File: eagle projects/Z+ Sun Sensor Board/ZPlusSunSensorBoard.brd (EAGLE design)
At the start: 91 x 91 mm, 53 parts, among them Q1 BSS138PS,115, Q2 BSS138PS,115, Q7 BSS138PS,115, Q8 BSS138PS,115, U1 ADS7841E_2K5, U2 REF194GSZ-REEL7, U3 TLV9054IDR, U4 LM20BIM7X_NOPB

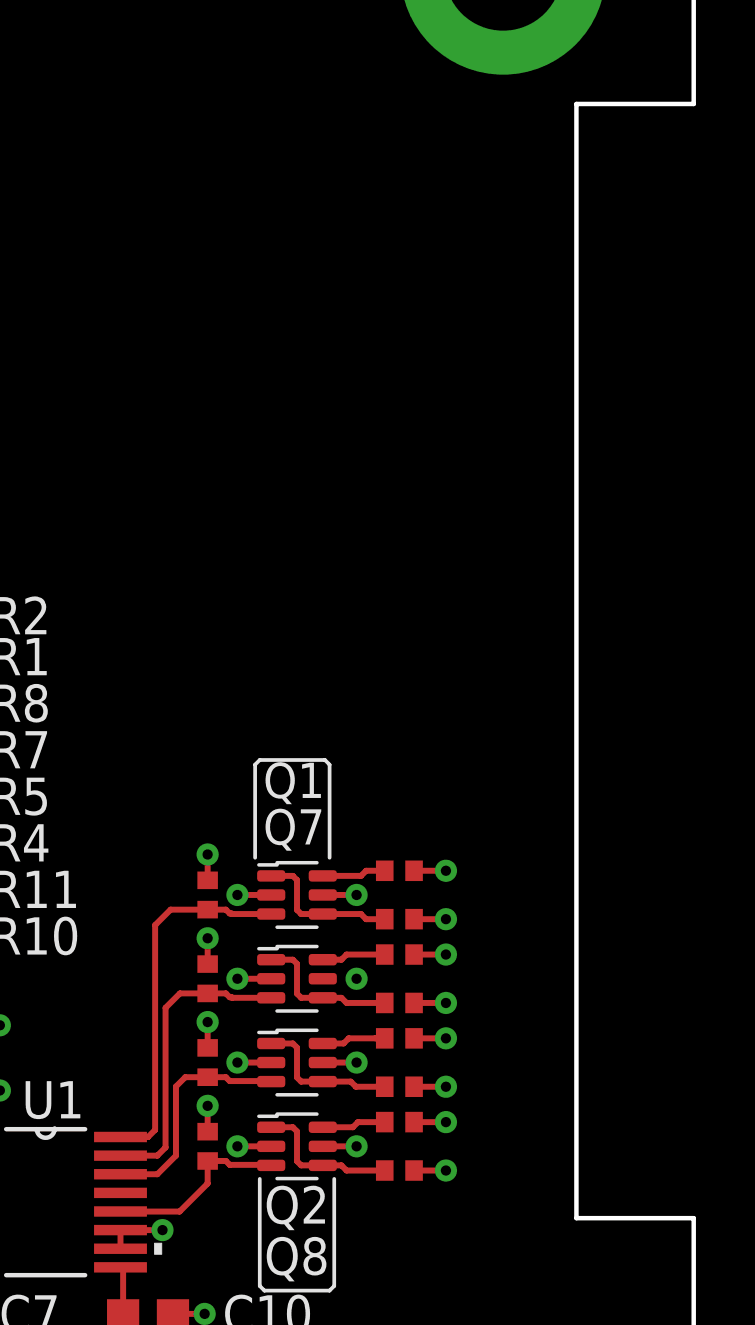
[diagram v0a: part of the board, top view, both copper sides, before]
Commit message: Added connector pins
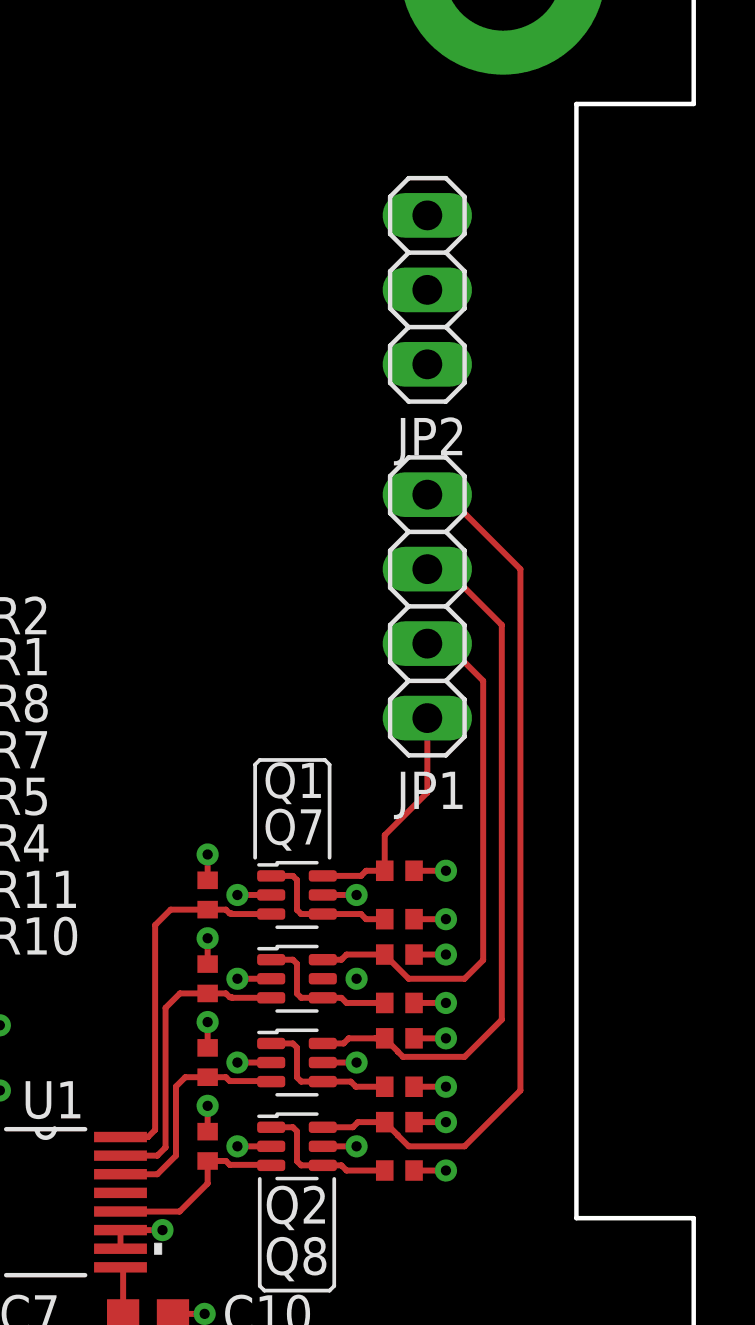
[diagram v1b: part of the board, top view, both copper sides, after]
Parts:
- added JP1: (no value), pinhead:1X04
- added JP2: (no value), pinhead:1X03
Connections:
- removed net !CS!_SUN_Z-: Q7.6, R8.1
- new net !CS!_SUN_Z+: JP1.2, Q7.6, R8.1
- net +3V3: now also JP2.2
- net +5V: now also JP2.1
- net GND: now also JP2.3
- net UCB0_SPI_CLK: now also JP1.1
- net UCB0_SPI_MISO: now also JP1.4
- net UCB0_SPI_MOSI: now also JP1.3
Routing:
- net UCB0_SPI_MISO: track 2.36 -> 30.1 mm
- net UCB0_SPI_MOSI: track 2.51 -> 24.1 mm
- net !CS!_SUN_Z+: track 0.00 -> 18.1 mm
- net UCB0_SPI_CLK: track 2.19 -> 7.99 mm
- net !CS!_SUN_Z-: track 2.19 -> 0.00 mm
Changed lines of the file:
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@@
 <setting verticaltext="up"/>
 </settings>
-<grid distance="12.5" unitdist="mil" unit="mil" style="lines" multiple="1" display="yes" altdistance="5" altunitdist="mil" altunit="mil"/>
+<grid distance="25" unitdist="mil" unit="mil" style="lines" multiple="1" display="yes" altdistance="5" altunitdist="mil" altunit="mil"/>
 <layers>
 <layer number="1" name="Top" color="4" fill="1" visible="yes" active="yes"/>
@@
 </layers>
 <board>
-<fusionsync huburn="a.YnVzaW5lc3M6bXlkYWwyMA" projecturn="a.YnVzaW5lc3M6bXlkYWwyMCMyMDE5MDkwNjIxMzMzMjg1MQ" f3durn="urn:adsk.wipprod:dm.lineage:9eKYqUHQRJ-z_v29RI24zA" pcbguid="613cd21b-15a5-4341-852d-328566686155" lastpulledtime="" lastsyncedchangeguid="" latestrevisionid="e225897c-414a-45e0-9606-f7f44216a340" lastsyncedrevisionid="e225897c-414a-45e0-9606-f7f44216a340" lastboardhashguid="898b3bb0-e8cf-4f41-3e9a-b056dcb77d80" lastpushedtime="2020-10-26T20:08:05Z" linktopcb3d="true"/>
+<fusionsync huburn="a.YnVzaW5lc3M6bXlkYWwyMA" projecturn="a.YnVzaW5lc3M6bXlkYWwyMCMyMDE5MDkwNjIxMzMzMjg1MQ" f3durn="urn:adsk.wipprod:dm.lineage:9eKYqUHQRJ-z_v29RI24zA" pcbguid="" lastpulledtime="" lastsyncedchangeguid="" latestrevisionid="e225897c-414a-45e0-9606-f7f44216a340" lastsyncedrevisionid="e225897c-414a-45e0-9606-f7f44216a340" lastboardhashguid="898b3bb0-e8cf-4f41-3e9a-b056dcb77d80" lastpushedtime="2020-10-26T20:08:05Z" linktopcb3d="true"/>
 <plain>
 <dimension x1="154.94" y1="86.995" x2="154.94" y2="13.335" x3="148.336" y3="50.165" textsize="3.5" layer="47"/>
@@
 <attribute name="SPICEPREFIX" value="C" x="57.15" y="33.9725" size="1.778" layer="27" rot="R270" display="off"/>
 </element>
+<element name="JP1" library="pinhead" library_urn="urn:adsk.eagle:library:325" package="1X04" package3d_urn="urn:adsk.eagle:package:22407/2" value="" x="81.915" y="62.865" smashed="yes" rot="R90">
+<attribute name="NAME" x="83.2612" y="57.2262" size="1.27" layer="25" ratio="10" rot="R180"/>
+<attribute name="POPULARITY" value="91" x="81.915" y="62.865" size="1.778" layer="27" rot="R90" display="off"/>
+<attribute name="VALUE" x="85.09" y="57.785" size="1.27" layer="27" rot="R90"/>
+</element>
+<element name="JP2" library="pinhead" library_urn="urn:adsk.eagle:library:325" package="1X03" package3d_urn="urn:adsk.eagle:package:22458/2" value="" x="81.915" y="73.66" smashed="yes" rot="R90">
+<attribute name="NAME" x="83.2612" y="69.2912" size="1.27" layer="25" ratio="10" rot="R180"/>
+<attribute name="POPULARITY" value="92" x="81.915" y="73.66" size="1.778" layer="27" rot="R90" display="off"/>
+<attribute name="VALUE" x="85.09" y="69.85" size="1.27" layer="27" rot="R90"/>
+</element>
 </elements>
 <signals>
@@
 <wire x1="66.255" y1="46.355" x2="66.3448" y2="46.2652" width="0.2032" layer="1"/>
 <wire x1="66.3448" y1="46.2652" x2="66.3448" y2="44.7675" width="0.2032" layer="1"/>
+<contactref element="JP2" pad="1"/>
 <wire x1="74.422" y1="51.5456" x2="74.422" y2="53.5225" width="0" layer="19" extent="1-1"/>
 <wire x1="74.422" y1="48.6881" x2="74.422" y2="50.665" width="0" layer="19" extent="1-1"/>
@@
 <wire x1="62.23" y1="21.07" x2="50.4825" y2="33.02" width="0" layer="19" extent="1-1"/>
 <wire x1="63.5" y1="21.07" x2="62.23" y2="21.07" width="0" layer="19" extent="1-1"/>
+<wire x1="81.915" y1="71.12" x2="50.4825" y2="33.02" width="0" layer="19" extent="1-1"/>
 </signal>
 <signal name="+3V3">
@@
 <wire x1="79.502" y1="44.45" x2="78.35" y2="44.45" width="0.2032" layer="1"/>
 <wire x1="82.55" y1="45.2755" x2="81.4625" y2="45.2755" width="0.2032" layer="1"/>
-<wire x1="82.55" y1="52.197" x2="82.55" y2="53.848" width="0" layer="19" extent="1-1"/>
+<contactref element="JP2" pad="2"/>
+<wire x1="81.4625" y1="52.197" x2="81.4625" y2="53.848" width="0" layer="19" extent="1-1"/>
 <wire x1="82.55" y1="50.9905" x2="82.55" y2="52.197" width="0" layer="19" extent="1-1"/>
 <wire x1="82.55" y1="49.3395" x2="82.55" y2="50.9905" width="0" layer="19" extent="1-1"/>
@@
 <wire x1="82.55" y1="45.2755" x2="82.55" y2="46.482" width="0" layer="19" extent="1-1"/>
 <wire x1="82.55" y1="43.6245" x2="82.55" y2="45.2755" width="0" layer="19" extent="1-1"/>
-<wire x1="79.502" y1="53.0225" x2="81.4625" y2="53.848" width="0" layer="19" extent="1-1"/>
-<wire x1="76.59" y1="53.0225" x2="78.35" y2="53.0225" width="0" layer="19" extent="1-1"/>
 <wire x1="79.502" y1="50.165" x2="81.4625" y2="50.9905" width="0" layer="19" extent="1-1"/>
 <wire x1="78.35" y1="50.165" x2="79.502" y2="50.165" width="0" layer="19" extent="1-1"/>
 <wire x1="76.59" y1="50.165" x2="78.35" y2="50.165" width="0" layer="19" extent="1-1"/>
+<wire x1="79.502" y1="53.0225" x2="81.4625" y2="53.848" width="0" layer="19" extent="1-1"/>
+<wire x1="76.59" y1="53.0225" x2="78.35" y2="53.0225" width="0" layer="19" extent="1-1"/>
 <wire x1="79.502" y1="47.3075" x2="81.4625" y2="48.133" width="0" layer="19" extent="1-1"/>
 <wire x1="76.59" y1="47.3075" x2="78.35" y2="47.3075" width="0" layer="19" extent="1-1"/>
 <wire x1="79.502" y1="44.45" x2="81.4625" y2="45.2755" width="0" layer="19" extent="1-1"/>
 <wire x1="76.59" y1="44.45" x2="78.35" y2="44.45" width="0" layer="19" extent="1-1"/>
+<wire x1="81.915" y1="73.66" x2="75.438" y2="44.45" width="0" layer="19" extent="1-1"/>
 </signal>
 <signal name="GND">
@@
 <wire x1="57.15" y1="33.1225" x2="57.15" y2="32.0419" width="0.2032" layer="1"/>
 <via x="57.15" y="32.0419" extent="1-16" drill="0.35"/>
+<contactref element="JP2" pad="3"/>
 <wire x1="73.24" y1="38.735" x2="71.4502" y2="40.9575" width="0" layer="19" extent="1-1"/>
 <wire x1="74.3206" y1="36.5125" x2="74.3206" y2="38.735" width="0" layer="19" extent="1-1"/>
@@
 <wire x1="23.9675" y1="42.22" x2="35.0875" y2="42.22" width="0" layer="19" extent="1-1"/>
 <wire x1="29.5275" y1="52.72" x2="35.0875" y2="42.22" width="0" layer="19" extent="1-1"/>
+<wire x1="81.915" y1="76.2" x2="23.9675" y2="42.22" width="0" layer="19" extent="1-1"/>
 </signal>
 <signal name="UCB0_SPI_CLK">
@@
 <wire x1="79.652" y1="53.6725" x2="79.8275" y2="53.848" width="0.2032" layer="1"/>
 <wire x1="80.4625" y1="53.848" x2="79.8275" y2="53.848" width="0.2032" layer="1"/>
+<contactref element="JP1" pad="1"/>
+<wire x1="80.4625" y1="53.848" x2="80.4625" y2="55.0625" width="0.2032" layer="1"/>
+<wire x1="81.915" y1="56.515" x2="81.915" y2="59.055" width="0.2032" layer="1"/>
+<wire x1="80.4625" y1="55.0625" x2="81.915" y2="56.515" width="0.2032" layer="1"/>
 </signal>
 <signal name="UCB0_SPI_MISO">
@@
 <wire x1="80.4625" y1="45.2755" x2="80.5895" y2="45.4025" width="0.2032" layer="1"/>
 <wire x1="79.5505" y1="45.2755" x2="80.4625" y2="45.2755" width="0.2032" layer="1"/>
+<contactref element="JP1" pad="4"/>
+<wire x1="80.4625" y1="45.2755" x2="80.9085" y2="44.8295" width="0.2032" layer="1"/>
+<wire x1="80.9085" y1="44.8295" x2="80.9085" y2="44.8202875" width="0.2032" layer="1"/>
+<wire x1="80.9085" y1="44.8202875" x2="81.2787875" y2="44.45" width="0.2032" layer="1"/>
+<wire x1="81.2787875" y1="44.45" x2="83.185" y2="44.45" width="0.2032" layer="1"/>
+<wire x1="85.09" y1="46.355" x2="83.185" y2="44.45" width="0.2032" layer="1"/>
+<wire x1="85.09" y1="64.135" x2="85.09" y2="46.355" width="0.2032" layer="1"/>
+<wire x1="81.915" y1="66.675" x2="82.55" y2="66.675" width="0.2032" layer="1"/>
+<wire x1="85.09" y1="64.135" x2="82.55" y2="66.675" width="0.2032" layer="1"/>
 </signal>
 <signal name="UCB0_SPI_MOSI">
@@
 <wire x1="80.4625" y1="48.133" x2="80.137" y2="48.133" width="0.2032" layer="1"/>
 <wire x1="80.4625" y1="48.133" x2="79.233" y2="48.133" width="0.2032" layer="1"/>
+<contactref element="JP1" pad="3"/>
+<wire x1="80.4625" y1="48.133" x2="80.9085" y2="47.687" width="0.2032" layer="1"/>
+<wire x1="80.9085" y1="47.687" x2="80.9085" y2="47.6777875" width="0.2032" layer="1"/>
+<wire x1="80.9085" y1="47.6777875" x2="81.0854875" y2="47.5008" width="0.2032" layer="1"/>
+<wire x1="81.0854875" y1="47.5008" x2="83.185" y2="47.5008" width="0.2032" layer="1"/>
+<wire x1="83.185" y1="47.5008" x2="84.455" y2="48.7708" width="0.2032" layer="1"/>
+<wire x1="84.455" y1="62.23" x2="84.455" y2="48.7708" width="0.2032" layer="1"/>
+<wire x1="84.455" y1="62.23" x2="82.55" y2="64.135" width="0.2032" layer="1"/>
+<wire x1="81.915" y1="64.135" x2="82.55" y2="64.135" width="0.2032" layer="1"/>
 </signal>
-<signal name="!CS!_SUN_Z-">
+<signal name="!CS!_SUN_Z+">
 <contactref element="Q7" pad="6"/>
 <contactref element="R8" pad="1"/>
@@
 <wire x1="79.1605" y1="50.9905" x2="78.985" y2="50.815" width="0.2032" layer="1"/>
 <wire x1="78.985" y1="50.815" x2="78.35" y2="50.815" width="0.2032" layer="1"/>
+<contactref element="JP1" pad="2"/>
+<wire x1="81.915" y1="61.595" x2="82.55" y2="61.595" width="0.2032" layer="1"/>
+<wire x1="83.82" y1="60.325" x2="82.55" y2="61.595" width="0.2032" layer="1"/>
+<wire x1="83.82" y1="50.8" x2="83.185" y2="50.165" width="0.2032" layer="1"/>
+<wire x1="81.2787875" y1="50.165" x2="80.4625" y2="50.9812875" width="0.2032" layer="1"/>
+<wire x1="80.4625" y1="50.9812875" x2="80.4625" y2="50.9905" width="0.2032" layer="1"/>
+<wire x1="83.82" y1="60.325" x2="83.82" y2="50.8" width="0.2032" layer="1"/>
+<wire x1="83.185" y1="50.165" x2="81.2787875" y2="50.165" width="0.2032" layer="1"/>
 </signal>
 <signal name="N$1">

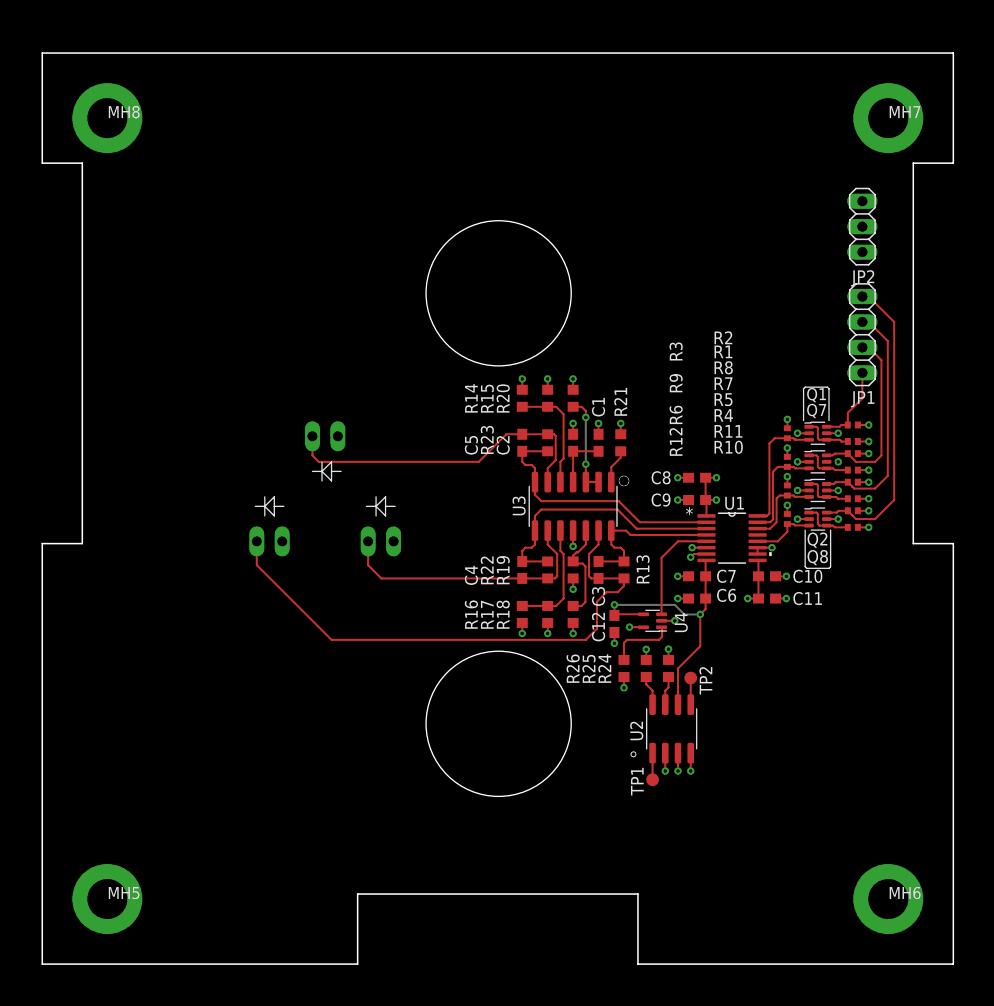
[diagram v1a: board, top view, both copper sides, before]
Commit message: Updated logic level shifter mosfet packages and board dimensions
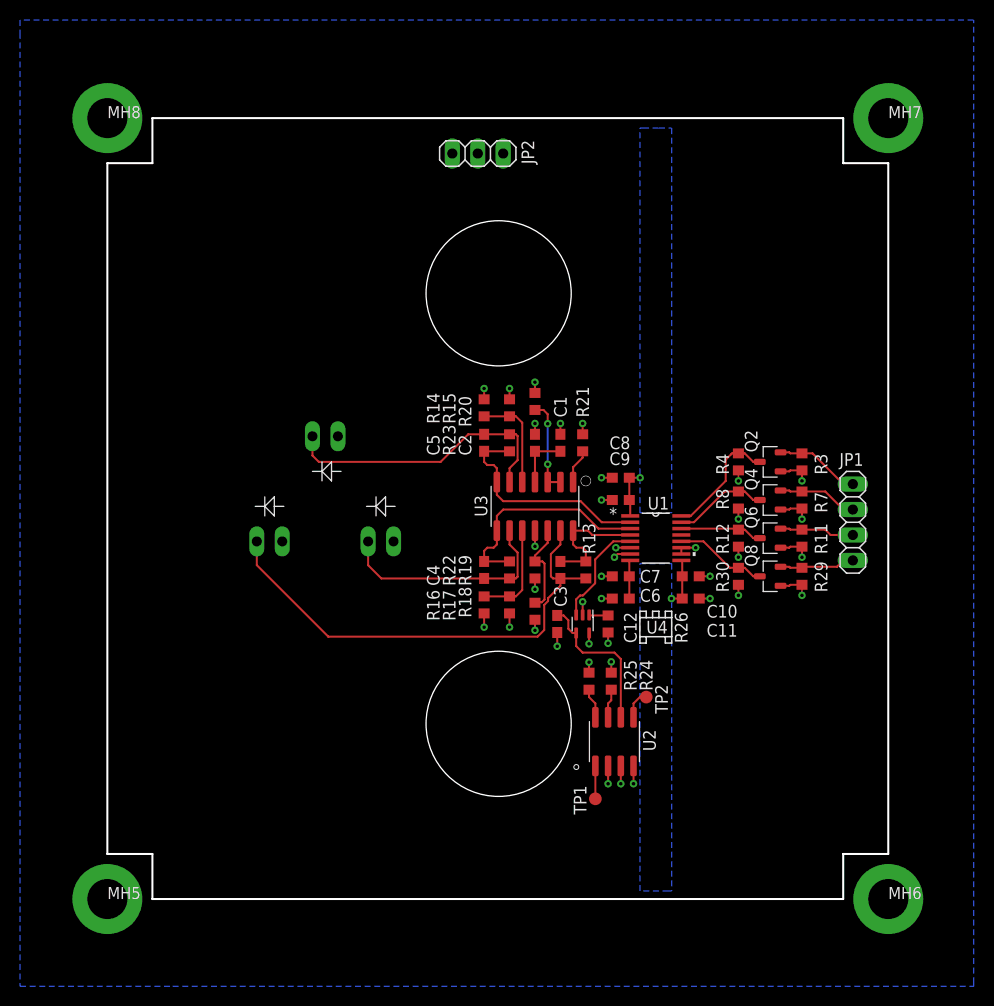
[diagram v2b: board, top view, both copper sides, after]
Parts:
- removed Q1, Q7: BSS138PS,115, my_library:SOT23-6P65_200X110L30X25N_BSS138PS,115
- removed R1, R10, R2, R5, R6, R9: 10k, rcl:R0402
- added Q4, Q6: BSS138, my_library:SOT23-3P95_237X111L42X43N_BSS138
- added R29, R30: 10k, rcl:R0603
- Q2, Q8: value BSS138PS,115 -> BSS138; device my_library:SOT23-6P65_200X110L30X25N_BSS138PS,115 -> my_library:SOT23-3P95_237X111L42X43N_BSS138
- R11, R12, R3, R4, R7, R8: device rcl:R0402 -> rcl:R0603
- moved JP2 39.1 mm to (43.5, 81.0), turned to 180 degrees
- moved JP1 18.8 mm to (81.0, 44.1), turned to 270 degrees
- moved R8 12.3 mm to (69.5, 46.4), turned to 270 degrees
- moved R4 12.0 mm to (69.5, 50.2), turned to 270 degrees
- moved C10 7.62 mm to (64.8, 38.7)
- moved C11 7.62 mm to (64.8, 36.5)
- moved C6 7.62 mm to (57.8, 36.5)
- moved C7 7.62 mm to (57.8, 38.7)
- moved C8 7.62 mm to (57.8, 48.6)
- moved C9 7.62 mm to (57.8, 46.4)
- moved U1 7.62 mm to (61.3, 42.5)
- moved Q8 7.44 mm to (72.7, 38.7), turned to 90 degrees
- moved U4 6.99 mm to (54.0, 34.0), turned to 180 degrees
- moved TP1 6.02 mm to (55.2, 16.5)
- moved R7 5.89 mm to (75.9, 46.4), turned to 270 degrees
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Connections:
- removed net N$1: Q1.1, Q1.4, R1.2
- removed net N$2: Q2.1, Q2.4, R4.2
- removed net N$3: Q7.1, Q7.4, R7.2
- removed net N$4: Q8.1, Q8.4, R10.2
- net !CS!_SUN_Z+: now also Q4.2, R7.1; no longer Q7.6, R8.1
- net +3V3: now also Q2.1, Q4.1, Q6.1, Q8.1, R29.2, R3.2, R7.2; no longer Q1.2, Q1.5, Q2.2, Q2.5, Q7.2, Q7.5, Q8.2, Q8.5, R1.1, R10.1, R2.2, R4.1, R5.2, R7.1, R8.2
- net +5V: now also R30.2, R4.2, R8.2; no longer R3.2, R6.2, R9.2
- net 5V_!CS!_SUN_Z-: now also Q4.3, R8.1; no longer Q7.3, R9.1
- net 5V_SPI_CLK: now also Q2.3, R4.1; no longer Q1.3, R3.1
- net 5V_SPI_MISO: now also R30.1; no longer R12.1
- net 5V_SPI_MOSI: now also Q6.3, R12.1; no longer Q2.3, R6.1
- net UCB0_SPI_CLK: now also Q2.2, R3.1; no longer Q1.6, R2.1
- net UCB0_SPI_MISO: now also Q8.2, R29.1; no longer Q8.6, R11.1
- net UCB0_SPI_MOSI: now also Q6.2, R11.1; no longer Q2.6, R5.1
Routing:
- net UCB0_SPI_MISO: track 30.1 -> 7.57 mm
- net UCB0_SPI_MOSI: track 24.1 -> 7.48 mm
- net !CS!_SUN_Z+: track 18.1 -> 8.01 mm
- net +4V5: track 28.6 -> 19.3 mm, vias 2 -> 0
- net N$15: track 54.5 -> 47.9 mm
- net N$4: track 5.08 -> 0.00 mm
- net N$2: track 5.08 -> 0.00 mm
- net N$3: track 5.08 -> 0.00 mm
- net N$1: track 5.08 -> 0.00 mm
- net N$7: track 6.72 -> 1.91 mm
- net N$14: track 26.9 -> 22.9 mm
- net +3V3: track 16.8 -> 12.9 mm, vias 16 -> 4
- net 120_DEGREES: track 26.2 -> 22.4 mm
- net 0_DEGREES: track 26.1 -> 22.2 mm
- net 240_DEGREES: track 16.2 -> 12.4 mm
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- added copper zone on layer 16, net GND
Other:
- board size 91 x 91 mm -> 78 x 78 mm
- board text removed: "Q3"
- board text removed: "Q4"
- board text removed: "Q5"
- board text removed: "Q6"
